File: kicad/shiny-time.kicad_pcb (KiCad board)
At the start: 2 copper layers, 100 x 100 mm, 44 parts, among them J1 Adafruit USB-C Power-Only Jac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, J2 Raspberry Pi Zero 2W, J3 QWIIC Connector, J4 JST-XH Buttons, J5 JST-XH Setup Button, J6 JST-XH Spare, J7 Conn_01x03_Pin, Q1 BS170, Q2 BS170, Q3 2N7000, U1 LD1117V33, U2 MCP23017x-x-SP, U3 TCA9517D, U4 DS1307+, Y1 32.768kHz

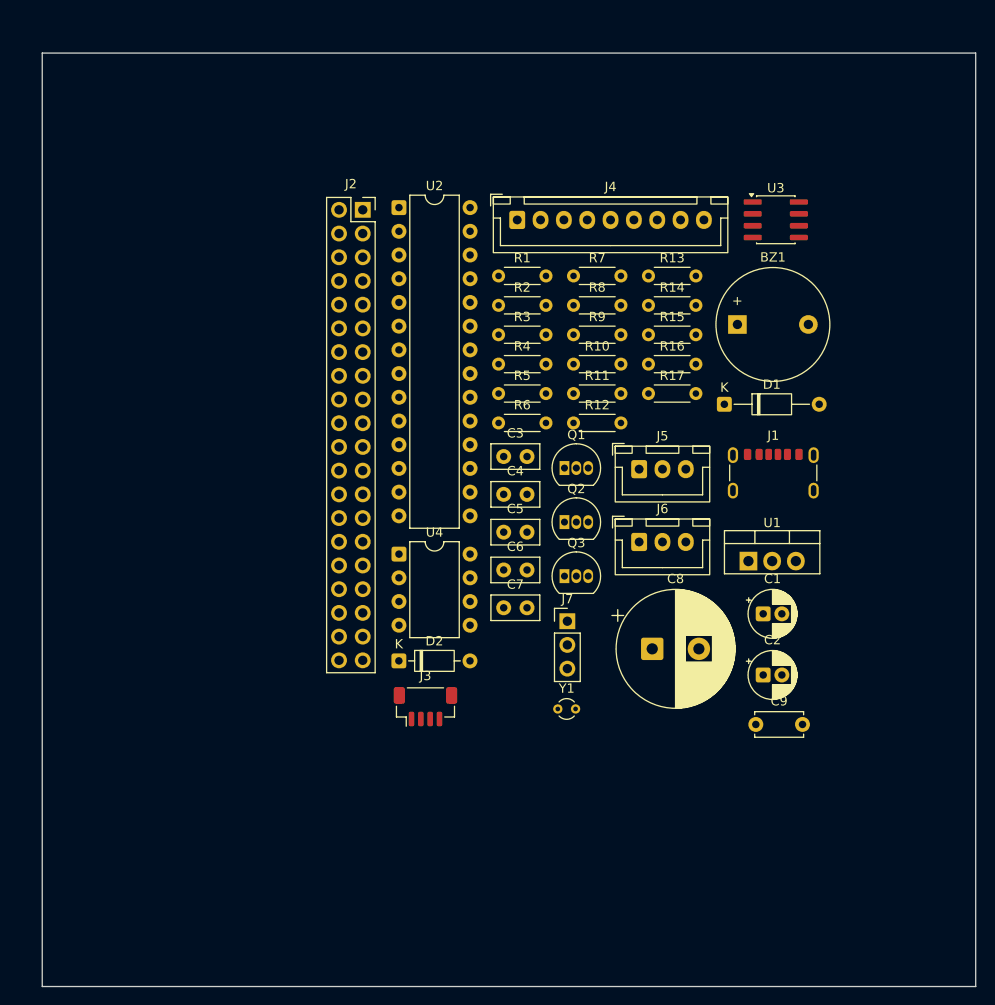
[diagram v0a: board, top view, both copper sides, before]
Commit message: Add pi holes
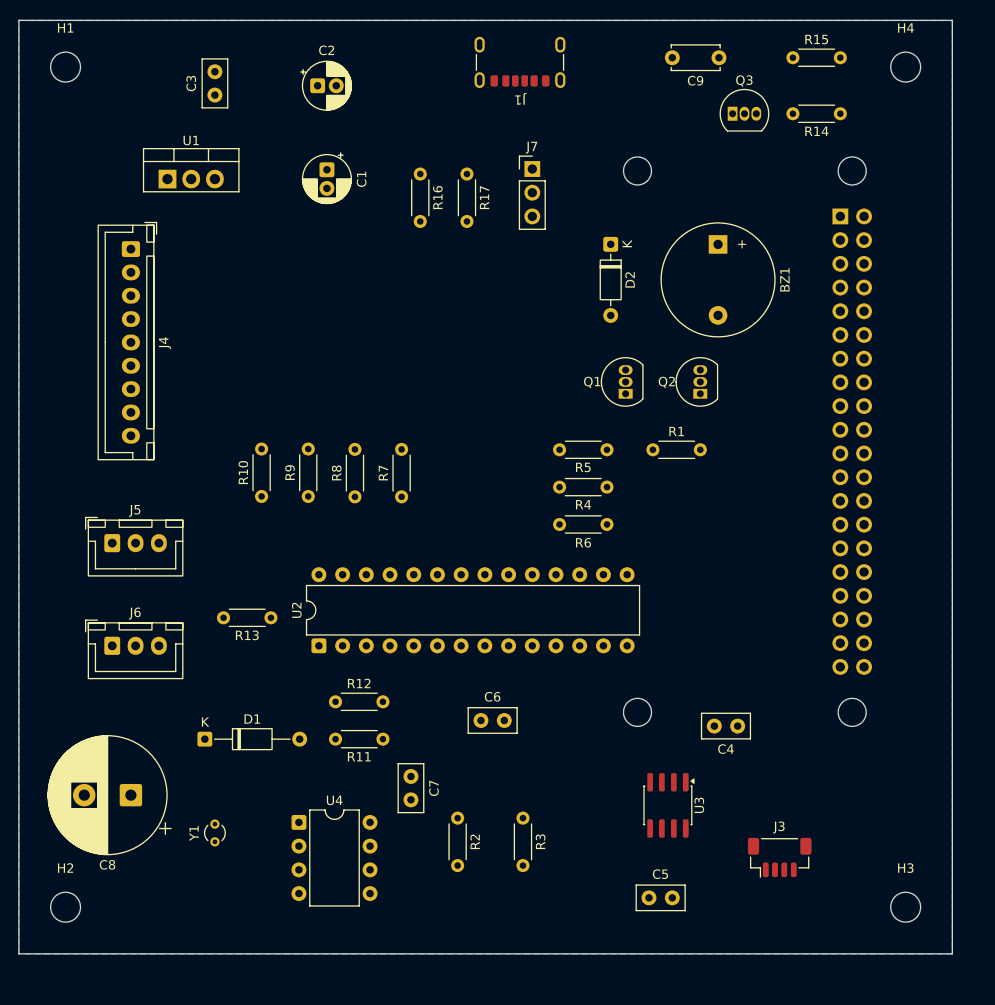
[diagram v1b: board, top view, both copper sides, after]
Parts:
- added H1: MountingHole_3.2mm_M3, MountingHole:MountingHole_3.2mm_M3, F.Cu at (55.0, 25.0)
- added H1: MountingHole_3mm, MountingHole:MountingHole_3mm, B.Cu at (139.3, 36.1)
- added H2: MountingHole_3.2mm_M3, MountingHole:MountingHole_3.2mm_M3, F.Cu at (55.0, 115.0)
- added H2: MountingHole_3mm, MountingHole:MountingHole_3mm, B.Cu at (139.3, 94.1)
- added H3: MountingHole_3.2mm_M3, MountingHole:MountingHole_3.2mm_M3, F.Cu at (145.0, 115.0)
- added H3: MountingHole_3mm, MountingHole:MountingHole_3mm, B.Cu at (116.3, 36.1)
- added H4: MountingHole_3.2mm_M3, MountingHole:MountingHole_3.2mm_M3, F.Cu at (145.0, 25.0)
- added H4: MountingHole_3mm, MountingHole:MountingHole_3mm, B.Cu at (116.3, 94.1)
- J2: moved to B.Cu
- moved C2 79.1 mm to (82.0, 27.0)
- moved U1 74.5 mm to (65.9, 37.0)
- moved C9 71.5 mm to (125.0, 24.0), turned to 180 degrees
- moved C1 66.7 mm to (83.0, 36.0), turned to -90 degrees
- moved D1 66.2 mm to (69.9, 97.0)
- moved U3 63.8 mm to (119.5, 104.1), turned to -90 degrees
- moved C8 58.0 mm to (62.0, 103.0), turned to 180 degrees
- moved J6 57.5 mm to (60.0, 87.0)
- moved J5 57.0 mm to (60.0, 76.0)
- moved R2 55.1 mm to (97.0, 105.5), turned to -90 degrees
- moved R13 54.6 mm to (77.0, 84.0), turned to 180 degrees
- moved J1 53.6 mm to (103.7, 23.4), turned to 180 degrees
- moved Q3 52.7 mm to (126.5, 30.0)
- moved R3 51.9 mm to (104.0, 105.5), turned to -90 degrees
- moved J2 51.2 mm to (138.0, 41.0), turned to 180 degrees
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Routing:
- added copper zone on B.Cu, net GND

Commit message: More schematic work
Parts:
- J2: footprint Connector_PinSocket_2.54mm:PinSocket_2x20_P2.54mm_Vertical -> Module:Raspberry_Pi_Zero_Socketed_THT_FaceDown_MountingHoles
- J7: value Conn_01x03_Pin -> SPDT; footprint Connector_PinHeader_2.54mm:PinHeader_1x03_P2.54mm_Vertical -> Button_Switch_THT:SW_E-Switch_EG1271_SPDT
- moved J7 10.4 mm to (101.9, 45.8)
- moved R16 2.95 mm to (90.2, 37.4)
- moved R17 2.30 mm to (95.9, 37.4)
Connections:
- J7 pad 1: +5V -> +3.3V
- J7 pad 3: +3.3V -> +5V
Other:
- board text added: "Shiny Time V1 For Sebs almostknown.com"

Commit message: More schematic work
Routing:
- net +3.3V: track 0.00 -> 236.8 mm, vias 0 -> 4
- net +5V: track 0.00 -> 140.7 mm
- net /3.3V_PI: track 0.00 -> 115.8 mm, vias 0 -> 4
- net /I2C_SDA_PI: track 0.00 -> 107.7 mm
- net /I2C_SDA_LOCAL: track 0.00 -> 81.0 mm
- net /I2C_SCL_LOCAL: track 0.00 -> 79.6 mm, vias 0 -> 3
- net /I2C_SDL_PI: track 0.00 -> 78.5 mm, vias 0 -> 2
- net /PI_PWM1: track 0.00 -> 59.4 mm
- net Net-(J4-Pin_1): track 0.00 -> 58.8 mm
- net Net-(J4-Pin_2): track 0.00 -> 56.1 mm
- net Net-(J4-Pin_3): track 0.00 -> 53.4 mm
- net Net-(Q2-D): track 0.00 -> 52.7 mm
- net Net-(J4-Pin_4): track 0.00 -> 52.1 mm
- net Net-(J5-Pin_2): track 0.00 -> 42.5 mm
- net GND: track 0.00 -> 41.8 mm
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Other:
- board text added: "Shiny Time V1 For Sebs almostknown.com Copyright (c) 2026 Almost Known"
- board text removed: "Shiny Time V1 For Sebs almostknown.com"
